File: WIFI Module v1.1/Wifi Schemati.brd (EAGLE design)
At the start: 90.1 x 63.4 mm, 25 parts, among them IC1 PIC24FVXXKA302-SP

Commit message: Moving Around Board
- Rotated ESP 180, fixed reprog issue
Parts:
- added SHORT_TO_RST: (no value), pinhead:1X01
- moved R4 54.5 mm to (85.5, 2.77)
- moved R5 54.3 mm to (85.5, 7.23), turned to 180 degrees
- moved TXPROG 40.1 mm to (12.0, 20.2), turned to 270 degrees
- moved RXPROG 39.9 mm to (14.4, 20.2), turned to 270 degrees
- moved S1 25.2 mm to (11.9, 12.6), turned to 0 degrees
- moved R2 24.6 mm to (22.5, 9.10), turned to 60 degrees
- moved U$1 14.2 mm to (16.2, -6.53), turned to 90 degrees
- moved R3 9.91 mm to (34.9, -12.7), turned to 0 degrees
- moved R6 5.59 mm to (34.7, -2.46), turned to 90 degrees
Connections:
- removed net N$3: R3.2, U$1.GPIO2
- new net N$12: R4.1, R5.1
- net 3.3V: no longer R4.1, R5.2
- net CLK: now also R3.2
- net FLSH_MD: no longer R4.2
- net MOSI: now also R4.2
- net N$1: now also SHORT_TO_RST.1; no longer R5.1
- net SS: now also R5.2
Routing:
- net GND: track 120.2 -> 172.2 mm, vias 4 -> 5
- net RXPIC: track 39.6 -> 65.9 mm, vias 0 -> 2
- net FLSH_MD: track 34.9 -> 9.06 mm
- net N$3: track 23.5 -> 0.00 mm, vias 1 -> 0
- net N$1: track 29.2 -> 6.54 mm, vias 1 -> 0
- net 3.3V: track 79.4 -> 58.4 mm
- net VDD: track 135.1 -> 127.9 mm, vias 2 -> 4
- net N$6: track 34.5 -> 40.2 mm
- net MCLR: track 46.4 -> 50.4 mm
- net TXPIC: track 44.8 -> 43.1 mm

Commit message: v1.1 PCB Changes
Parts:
- moved SV1 41.7 mm to (43.7, 15.7), turned to 0 degrees
- moved R1 38.3 mm to (72.2, -6.31)
- moved POWER 37.9 mm to (36.1, -13.9), turned to 0 degrees
- moved R3 37.4 mm to (72.3, -12.9), turned to 180 degrees
- moved RED_POWER 31.1 mm to (38.1, -5.73), turned to 90 degrees
- moved WIFI 30.4 mm to (42.5, -13.9), turned to 0 degrees
- moved BLUE_WIFI 25.2 mm to (41.2, -5.75), turned to 270 degrees
- moved SPI 24.1 mm to (48.8, -13.9), turned to 0 degrees
- moved R4 23.2 mm to (72.3, -16.3)
- moved R5 21.3 mm to (72.3, -9.48)
- moved GREEN_SPI 20.4 mm to (44.2, -5.73), turned to 270 degrees
- moved UART 19.9 mm to (55.1, -13.9), turned to 0 degrees
- moved SV2 17.4 mm to (64.7, -9.68)
- moved YELLOW_UART 17.0 mm to (47.2, -5.73), turned to 270 degrees
- moved TXOUT 14.9 mm to (65.2, 14.7)
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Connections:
- removed net N$12: R4.1, R5.1
- net 3.3V: no longer R3.1
- net VDD: now also R3.1, R4.1, R5.1
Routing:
- net GND: track 172.2 -> 92.6 mm, vias 5 -> 4
- net VDD: track 127.9 -> 106.5 mm, vias 4 -> 0
- net N$6: track 40.2 -> 20.0 mm
- net 3.3V: track 58.4 -> 39.4 mm
- net MOSI: track 12.8 -> 28.5 mm
- net CLK: track 12.2 -> 24.2 mm
- net SS: track 11.1 -> 22.2 mm
- net TXOUT: track 14.5 -> 3.90 mm
- net TXPIC: track 43.1 -> 51.5 mm
- net MISO: track 17.2 -> 25.3 mm
- net PGC: track 8.65 -> 15.0 mm, vias 0 -> 2
- net PGD: track 11.6 -> 5.59 mm
- net MCLR: track 50.4 -> 46.6 mm
- net TX: track 16.0 -> 12.4 mm
- net N$10: track 4.83 -> 8.41 mm
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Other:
- board size 90.1 x 63.4 mm -> 78.6 x 45.8 mm
- board text added: "WiFi 1.1"
- board text removed: "GND"
- board text removed: "WiFi 1.0"

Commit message: Changed angle of pull up R's
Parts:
- moved R1 2.66 mm to (72.0, -3.67), turned to 225 degrees
- moved R5 2.14 mm to (72.1, -7.35), turned to 225 degrees
- moved R3 1.76 mm to (72.1, -11.2), turned to 225 degrees
- moved R4 1.30 mm to (72.1, -15.0), turned to 225 degrees
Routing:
- net MCLR: track 46.6 -> 41.8 mm
- net MOSI: track 28.5 -> 30.1 mm
- net CLK: track 24.2 -> 25.5 mm
- net VDD: track 106.5 -> 105.3 mm
- net SS: track 22.2 -> 23.2 mm

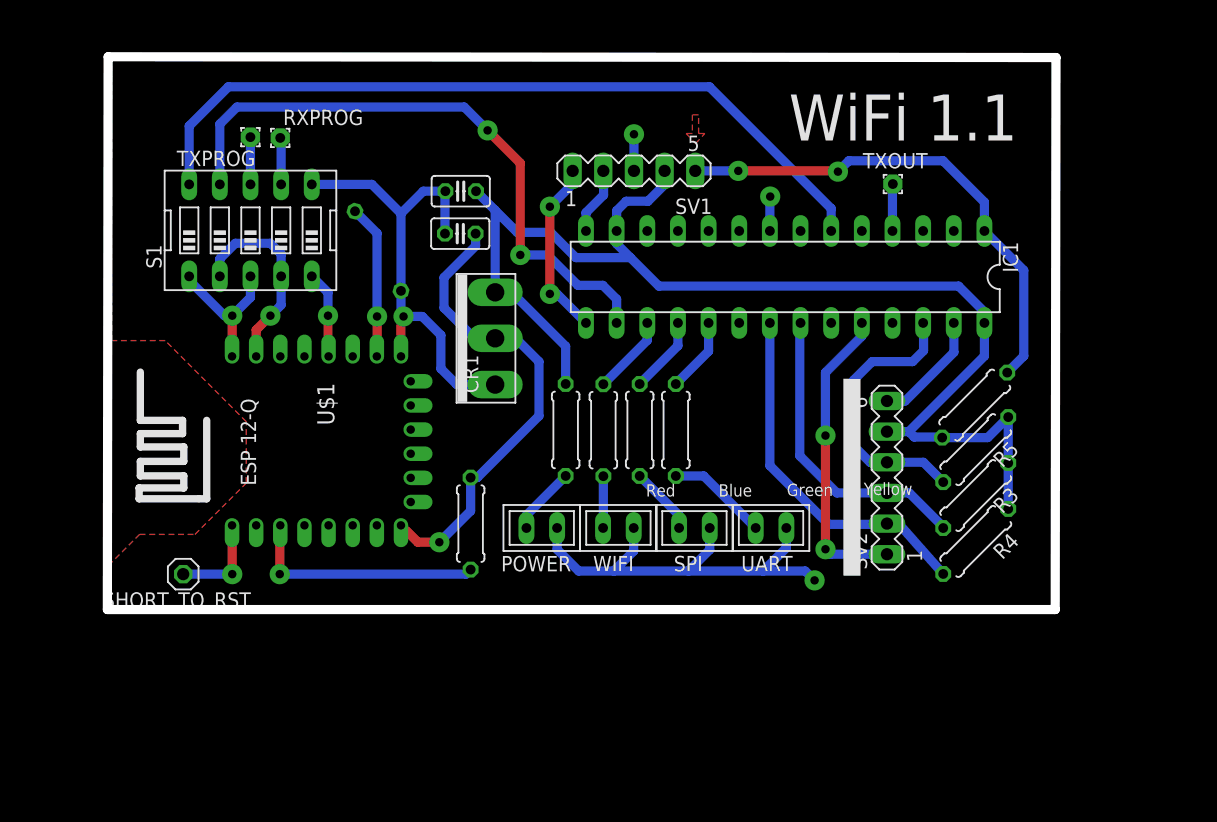
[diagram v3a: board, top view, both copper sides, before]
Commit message: Update PCB, 3V3.lbr, and grbs
Made edits to PCB after milling v1.1
Updated 3v3.lbr footprint
Added gerbers from latest mill
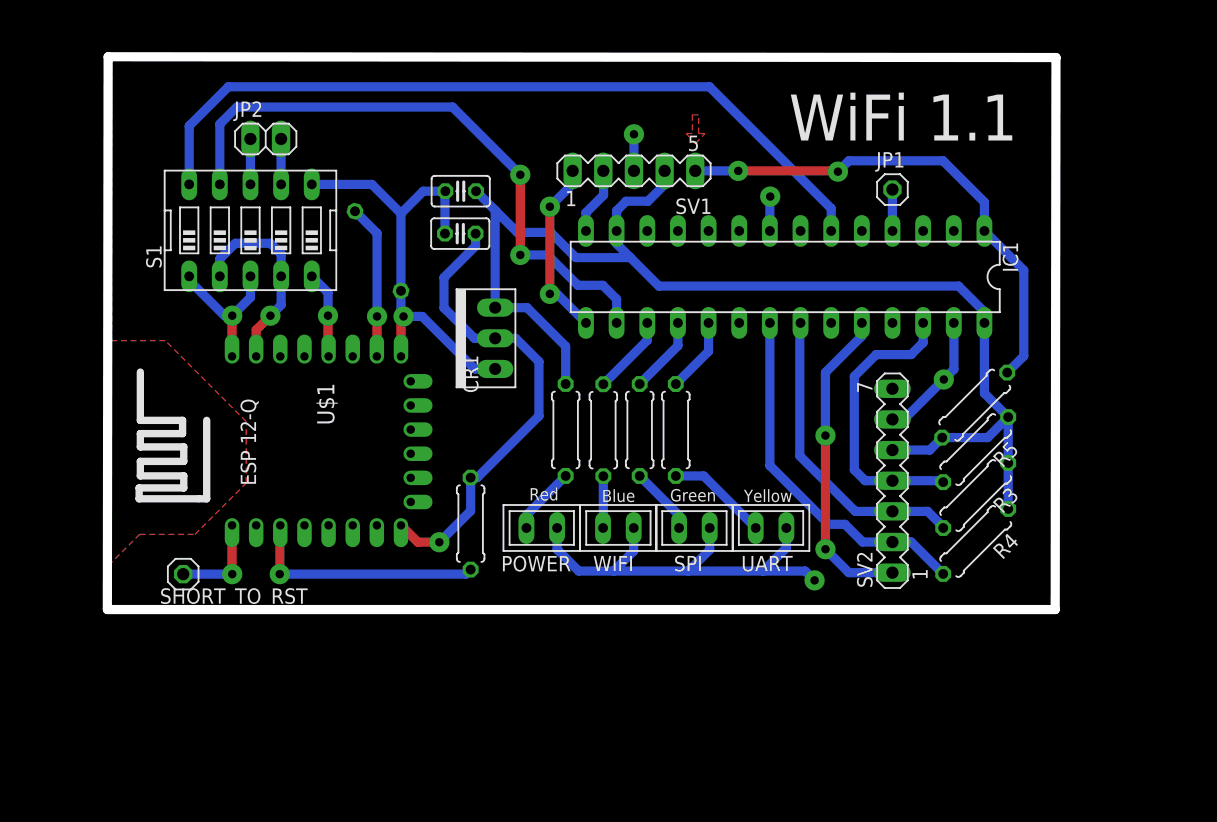
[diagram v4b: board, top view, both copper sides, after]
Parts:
- removed RXPROG, TXOUT, TXPROG: (no value), wirepad:1,6/0,8
- added JP1: (no value), pinhead:1X01
- added JP2: (no value), pinhead:1X02
- SV2: device con-lstb:MA06-1 -> con-lstb:MA07-1
- moved SV2 0.52 mm to (65.2, -9.94)
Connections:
- removed net N$4: S1.8, TXPROG.1
- removed net N$5: RXPROG.1, S1.7
- new net +12V: SV2.7
- new net RXPROG: JP2.2, S1.7
- new net TXPROG: JP2.1, S1.8
- net TXOUT: now also JP1.1; no longer TXOUT.1
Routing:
- net N$4: track 3.92 -> 0.00 mm
- net N$5: track 3.88 -> 0.00 mm
- net TXPROG: track 0.00 -> 3.77 mm
- net RXPROG: track 0.00 -> 3.77 mm
- net VDD: track 105.3 -> 102.9 mm
- net MISO: track 25.3 -> 26.9 mm
- net GND: track 92.6 -> 91.4 mm, vias 4 -> 5
- net SS: track 23.2 -> 24.0 mm
- net TXPIC: track 51.5 -> 50.9 mm
